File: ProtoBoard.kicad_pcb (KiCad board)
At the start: 4 copper layers, 68.2 x 45 mm, 56 parts, among them J1 Conn_01x02_Female, J10 Conn_01x06_Female, J2 Conn_01x10_Female, J3 I2C_STANDARDQWIIC, J4 Conn_01x10_Female, J5 Conn_01x05_Female, J6 Conn_01x05_Female, J7 Conn_01x10_Female, J8 Conn_01x05_Female, J9 Conn_01x10_Female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

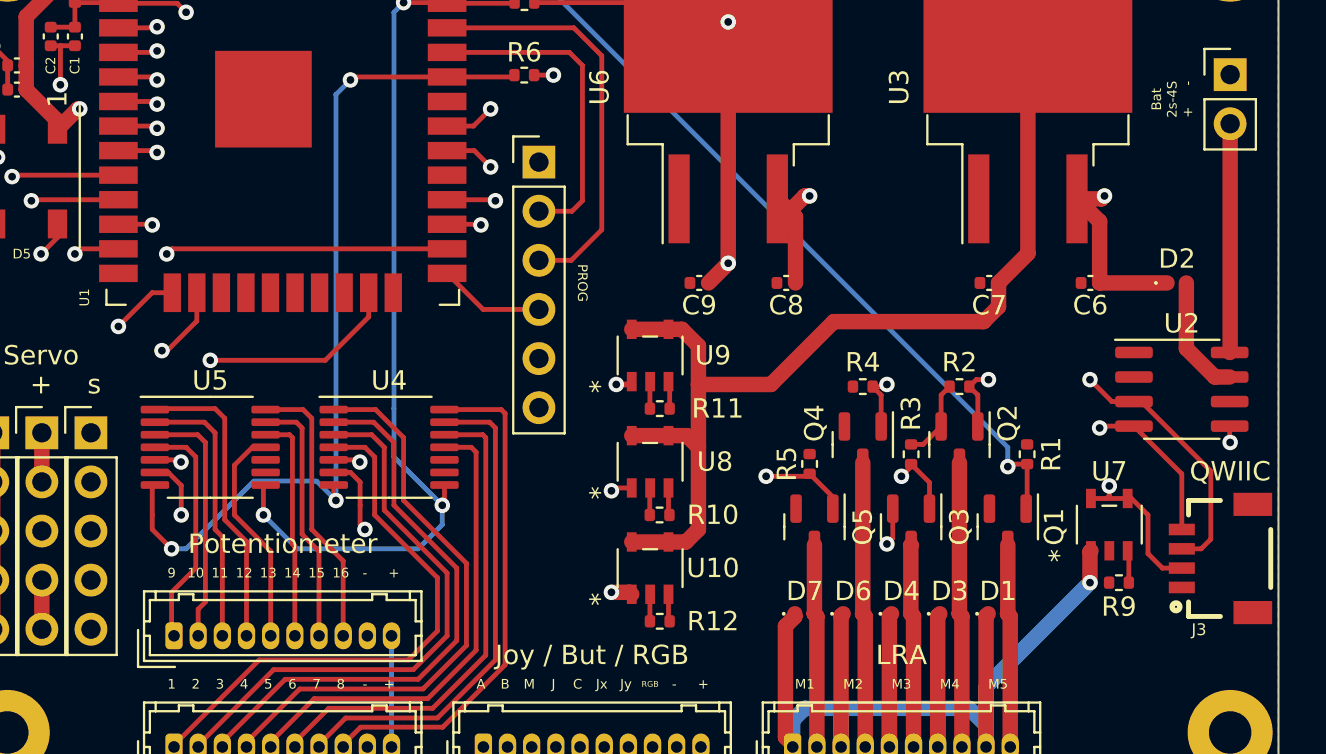
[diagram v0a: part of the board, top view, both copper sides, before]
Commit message: add shunt resistor and set i2c addresses
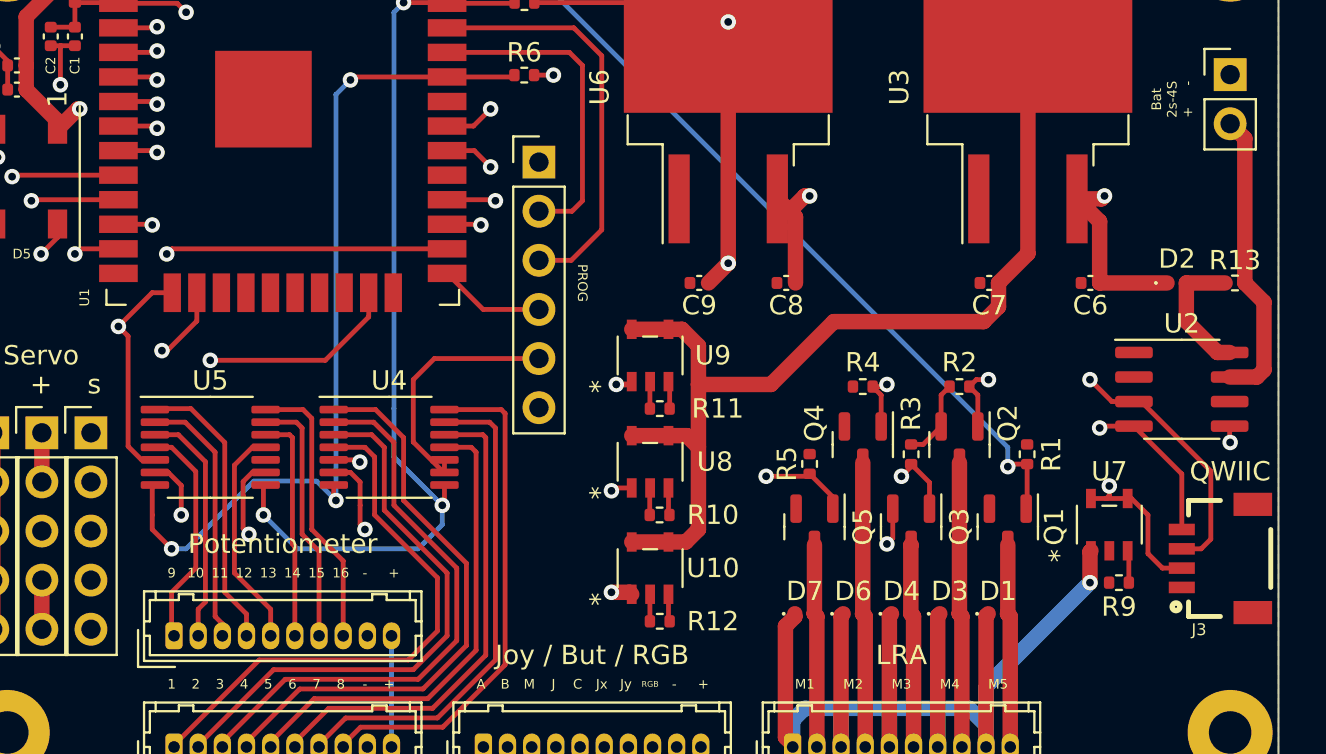
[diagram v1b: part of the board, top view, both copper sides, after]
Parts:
- added R13: 0.01R, Resistor_SMD:R_0402_1005Metric, F.Cu at (123.5, 69.2)
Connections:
- D2 pad 2: Net-(D2-Pad2) -> Net-(U2-Pad8)
- J1 pad 2: Net-(J1-Pad2) -> Net-(U2-Pad7)
- U2 pad 1: unconnected-(U2-Pad1) -> GND
- U2 pad 2: unconnected-(U2-Pad2) -> GND
- U2 pad 7: Net-(D2-Pad2) -> Net-(U2-Pad7)
- U2 pad 8: Net-(J1-Pad2) -> Net-(U2-Pad8)
- U4 pad 10: unconnected-(U4-Pad10) -> GND
- U4 pad 9: unconnected-(U4-Pad9) -> GND
- U5 pad 9: unconnected-(U5-Pad9) -> GND
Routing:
- net GND: track 34.4 -> 58.4 mm
- net Net-(U2-Pad7): track 0.00 -> 15.4 mm
- net Net-(J1-Pad2): track 11.8 -> 0.00 mm
- net Net-(U2-Pad8): track 0.00 -> 6.90 mm
- net Net-(D2-Pad2): track 6.24 -> 0.00 mm
- net /CH12: track 15.6 -> 14.8 mm
- net /CH11: track 14.0 -> 13.4 mm
- net /CH10: track 12.9 -> 12.3 mm

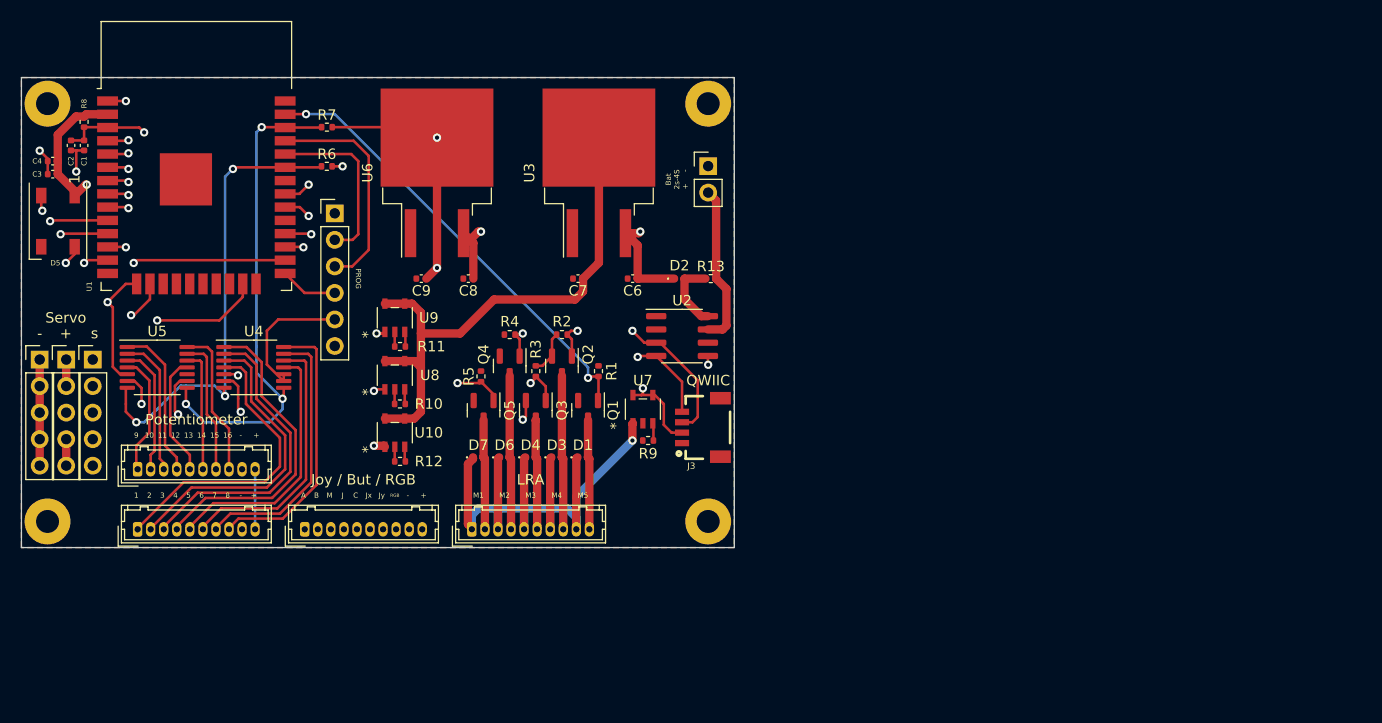
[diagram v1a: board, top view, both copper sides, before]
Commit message: smaller (but more expensive) version board
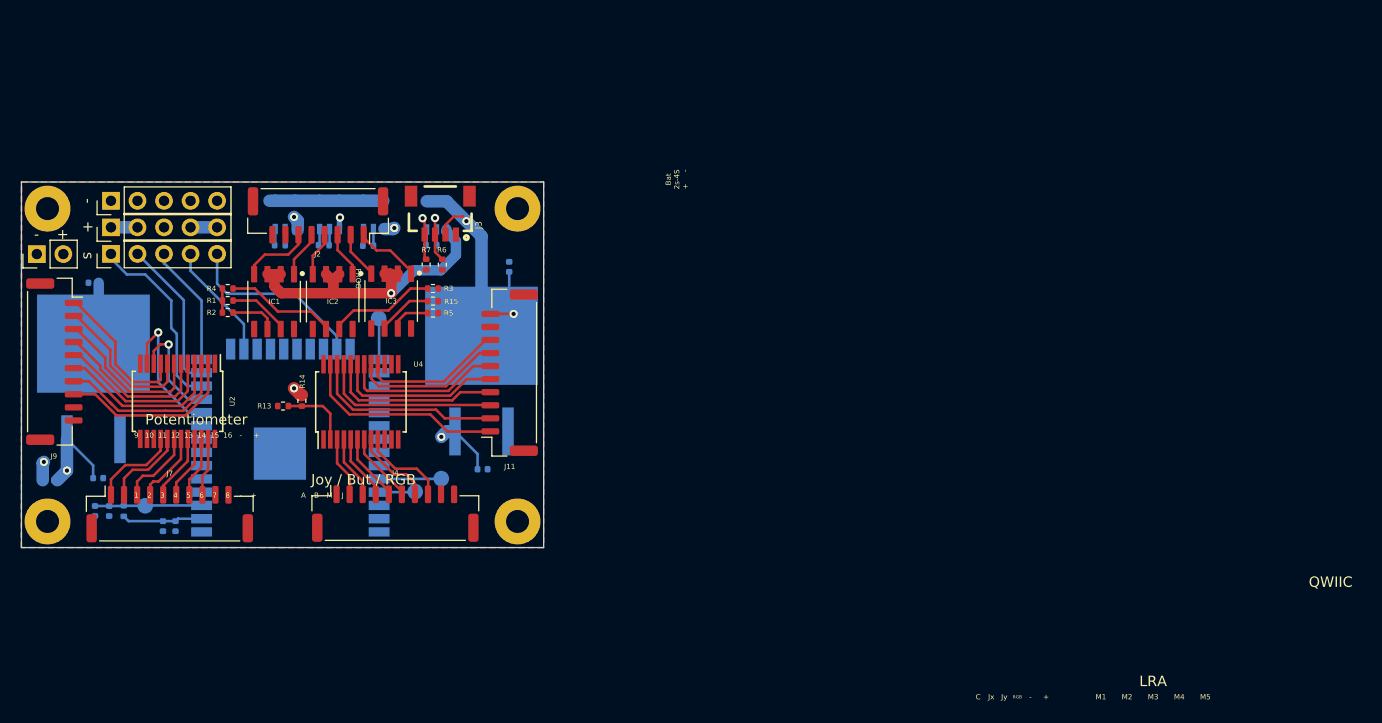
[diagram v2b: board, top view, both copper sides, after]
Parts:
- removed D1, D3, D4, D6, D7: D, Diode_SMD:D_0402_1005Metric
- removed D5: WS2812B, LED_SMD:LED_WS2812B_PLCC4_5.0x5.0mm_P3.2mm
- removed J10: Conn_01x06_Female, Connector_PinHeader_2.54mm:PinHeader_1x06_P2.54mm_Vertical
- removed Q1, Q2, Q3, Q4, Q5: 2N7002, Package_TO_SOT_SMD:SOT-23
- removed U5: MCP3428, Package_SO:TSSOP-14_4.4x5mm_P0.65mm
- added IC1: L9110S, footprints:SOIC127P600X150-8, F.Cu at (81.7, 71.5)
- added IC2: L9110S, footprints:SOIC127P600X150-8, F.Cu at (87.3, 71.5)
- added IC3: L9110S, footprints:SOIC127P600X150-8, F.Cu at (92.9, 71.4)
- added J11: Conn_01x10_Female, Connector_JST:JST_GH_SM10B-GHS-TB_1x10-1MP_P1.25mm_Horizontal, F.Cu at (104.2, 78.2)
- added R14: 1M, Resistor_SMD:R_0402_1005Metric, F.Cu at (84.3, 81.0)
- added R15: 10K, Resistor_SMD:R_0402_1005Metric, F.Cu at (96.9, 71.4)
- added TP1: TestPoint, TestPoint:TestPoint_Pad_D1.5mm, B.Cu at (69.3, 91.0)
- added TP2: TestPoint, TestPoint:TestPoint_Pad_D1.5mm, B.Cu at (97.7, 88.4)
- added TP3: TestPoint, TestPoint:TestPoint_Pad_D1.5mm, B.Cu at (95.2, 89.7)
- added TP4: TestPoint, TestPoint:TestPoint_Pad_D1.5mm, B.Cu at (91.7, 73.0)
- C1, C2, C3, C4, C6, C7, C8, C9, D2, R10, R11, R12, R8, R9, U1, U10, U3, U6, U7, U8, U9: moved to B.Cu
- J2: value Conn_01x10_Female -> Conn_01x08_Female; footprint Connector_Hirose:Hirose_DF13-10P-1.25DSA_1x10_P1.25mm_Vertical -> Connector_JST:JST_GH_SM08B-GHS-TB_1x08-1MP_P1.25mm_Horizontal
- J4, J7, J9: footprint Connector_Hirose:Hirose_DF13-10P-1.25DSA_1x10_P1.25mm_Vertical -> Connector_JST:JST_GH_SM10B-GHS-TB_1x10-1MP_P1.25mm_Horizontal
- R1, R2, R3, R4, R5: value 100K -> 10K
- R13: value 0.01R -> 6M
- U2: value INA219AxD -> CD74HC4067SM; footprint Package_SO:SOIC-8_3.9x4.9mm_P1.27mm -> Package_SO:SSOP-24_5.3x8.2mm_P0.65mm
- U4: value MCP3428 -> CD74HC4067SM; footprint Package_SO:TSSOP-14_4.4x5mm_P0.65mm -> Package_SO:SSOP-24_5.3x8.2mm_P0.65mm
- moved J1 64.8 mm to (59.0, 66.9), turned to 90 degrees
- moved D2 63.4 mm to (60.1, 88.5), turned to 180 degrees
- moved C6 54.6 mm to (64.8, 88.3), turned to 0 degrees
- moved U3 52.3 mm to (64.4, 78.8)
- moved U2 48.7 mm to (72.5, 81.0), turned to -90 degrees
- moved C7 46.4 mm to (64.4, 69.7)
- moved R13 42.7 mm to (82.5, 81.5), turned to 180 degrees
- moved R8 37.5 mm to (67.3, 91.5), turned to 90 degrees
- moved C4 36.5 mm to (71.0, 93.0), turned to -90 degrees
- moved R1 36.1 mm to (77.2, 71.3), turned to 180 degrees
- moved C3 35.7 mm to (72.2, 93.0), turned to -90 degrees
- moved C2 35.2 mm to (65.9, 91.5)
- moved C1 35.0 mm to (64.5, 91.5)
- moved J2 33.5 mm to (85.9, 63.2), turned to 180 degrees
- moved R2 32.1 mm to (77.2, 72.5)
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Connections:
- D2 pad 2: Net-(U2-Pad8) -> Net-(D2-Pad2)
- J1 pad 2: Net-(U2-Pad7) -> Net-(D2-Pad2)
- J2 pad 1: /POWER4 -> /M1+
- J2 pad 2: /M1- -> /M2+
- J2 pad 3: /POWER4 -> /M3+
- J2 pad 4: /M2- -> /M4+
- J2 pad 5: /POWER4 -> /M5+
- J2 pad 6: /M3- -> /M6+
- J2 pad 7: /POWER4 -> GND
- J2 pad 8: /M4- -> GND
- J4 pad 1: /ButA -> /RGB
- J4 pad 2: Net-(D5-Pad2) -> /ButA
- J7 pad 1: /CH1 -> /CH16
- J7 pad 2: /CH2 -> /CH15
- J7 pad 3: /CH3 -> /CH14
- J7 pad 4: /CH4 -> /CH13
- J7 pad 5: /CH5 -> /CH12
- J7 pad 6: /CH6 -> /CH11
- J7 pad 7: /CH7 -> /CH10
- J7 pad 8: /CH8 -> /CH9
- J8 pad 1: /S9 -> /S11
- J9 pad 1: /CH9 -> /CH1
- J9 pad 2: /CH10 -> /CH2
- J9 pad 3: /CH11 -> /CH3
- J9 pad 4: /CH12 -> /CH4
- J9 pad 5: /CH13 -> /CH5
- J9 pad 6: /CH14 -> /CH6
- J9 pad 7: /CH15 -> /CH7
- J9 pad 8: /CH16 -> /CH8
- R1 pad 2: GND -> +3V3
- R13 pad 1: Net-(U2-Pad8) -> Net-(R13-Pad1)
- R13 pad 2: Net-(U2-Pad7) -> GND
- R2 pad 1: /S7 -> /S9
- R2 pad 2: GND -> +3V3
- R3 pad 2: GND -> +3V3
- R4 pad 1: /S5 -> /S7
- R4 pad 2: GND -> +3V3
- R5 pad 2: GND -> +3V3
- U1 pad 10: /S9 -> /SEL2
- U1 pad 11: /S10 -> /SEL1
- U1 pad 12: /ButA -> /S11
- U1 pad 13: /S2 -> /S10
- U1 pad 14: unconnected-(U1-Pad14) -> /S2
- U1 pad 29: unconnected-(U1-Pad29) -> /S9
- U1 pad 4: /JoyX -> unconnected-(U1-Pad4)
- U1 pad 5: /JoyY -> unconnected-(U1-Pad5)
- U1 pad 6: /ButJ -> unconnected-(U1-Pad6)
- U1 pad 7: /ButC -> unconnected-(U1-Pad7)
- U1 pad 8: /ButB -> /SEL3
- U1 pad 9: /Menu -> /SEL4
- U2 pad 2: GND -> /CH8
- U2 pad 3: /I2C_SDA -> /CH7
- U2 pad 4: /I2C_SCL -> /CH6
- U2 pad 5: +3V3 -> /CH5
- U2 pad 6: GND -> /CH4
- U2 pad 7: Net-(U2-Pad7) -> /CH3
- U2 pad 8: Net-(U2-Pad8) -> /CH2
- U4 pad 1: /CH4 -> GND
- U4 pad 10: GND -> /SEL1
- U4 pad 11: /CH5 -> /SEL2
- U4 pad 12: /CH6 -> GND
- U4 pad 13: /CH7 -> /SEL4
- U4 pad 14: /CH8 -> /SEL3
- U4 pad 2: /CH3 -> Net-(R13-Pad1)
- U4 pad 3: /CH2 -> /ButA
- U4 pad 4: /CH1 -> /Menu
- U4 pad 5: GND -> /ButB
- U4 pad 6: +3V3 -> /ButC
- U4 pad 7: /I2C_SDA -> /ButJ
- U4 pad 8: /I2C_SCL -> /JoyY
- U4 pad 9: GND -> /JoyX
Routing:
- net +3V3: track 211.3 -> 39.2 mm, vias 8 -> 2
- net /I2C_SDA: track 105.4 -> 4.24 mm, vias 4 -> 1
- net /I2C_SCL: track 104.3 -> 4.06 mm, vias 4 -> 1
- net /POWER4: track 103.2 -> 33.2 mm
- net GND: track 58.4 -> 6.22 mm, vias 7 -> 0
- net Net-(D5-Pad2): track 47.0 -> 0.00 mm, vias 1 -> 0
- net /JoyX: track 49.9 -> 8.46 mm, vias 1 -> 0
- net /JoyY: track 48.1 -> 7.66 mm, vias 1 -> 0
- net /ButJ: track 46.1 -> 6.74 mm, vias 1 -> 0
- net +5V: track 60.4 -> 21.6 mm
- net /ButC: track 44.4 -> 6.49 mm, vias 1 -> 0
- net /S8: track 43.4 -> 5.92 mm, vias 2 -> 0
- net /ButB: track 42.6 -> 6.24 mm, vias 1 -> 0
- net /Menu: track 40.8 -> 6.00 mm, vias 1 -> 0
- net /ButA: track 36.7 -> 5.75 mm, vias 1 -> 0
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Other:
- board size 68.2 x 45 mm -> 50 x 35 mm
- board text removed: "Servo"

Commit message: Board cleaning progress
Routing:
- net +3V3: track 39.2 -> 144.3 mm, vias 2 -> 4
- net /SEL3: track 0.00 -> 69.0 mm, vias 0 -> 2
- net /RGB: track 0.00 -> 56.6 mm, vias 0 -> 2
- net /SEL4: track 0.00 -> 52.2 mm, vias 0 -> 4
- net GND: track 6.22 -> 47.9 mm, vias 0 -> 8
- net /I2C_SCL: track 4.06 -> 41.5 mm, vias 1 -> 2
- net /I2C_SDA: track 4.24 -> 38.6 mm, vias 1 -> 2
- net /SEL2: track 13.6 -> 46.0 mm, vias 1 -> 2
- net /S8: track 5.92 -> 37.4 mm, vias 0 -> 2
- net /S7: track 10.6 -> 41.1 mm, vias 0 -> 1
- net /SEL1: track 10.2 -> 36.1 mm, vias 1 -> 2
- net +5V: track 21.6 -> 46.1 mm
- net /S4: track 3.88 -> 25.9 mm, vias 0 -> 2
- net /S5: track 5.35 -> 22.8 mm, vias 0 -> 1
- net /S6: track 10.3 -> 26.3 mm, vias 0 -> 1
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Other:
- board text removed: "1"
- board text removed: "10"
- board text removed: "11"
- board text removed: "12"
- board text removed: "13"
- board text removed: "14"
- board text removed: "15"
- board text removed: "16"
- board text removed: "2"
- board text removed: "3"
- board text removed: "4"
- board text removed: "5"
- board text removed: "6"
- board text removed: "7"
- board text removed: "8"
- board text removed: "9"
- board text removed: "A"
- board text removed: "B"
- board text removed: "Bat 2s-4S + -"
- board text removed: "C"
- board text removed: "J"
- board text removed: "Joy / But / RGB"
- board text removed: "Jx"
- board text removed: "Jy"
- board text removed: "LRA"
- board text removed: "M"
- board text removed: "M1"
- board text removed: "M2"
- board text removed: "M3"
- board text removed: "M4"
- board text removed: "M5"
- board text removed: "PROG"
- board text removed: "Potentiometer"
- board text removed: "QWIIC"
- board text removed: "RGB"

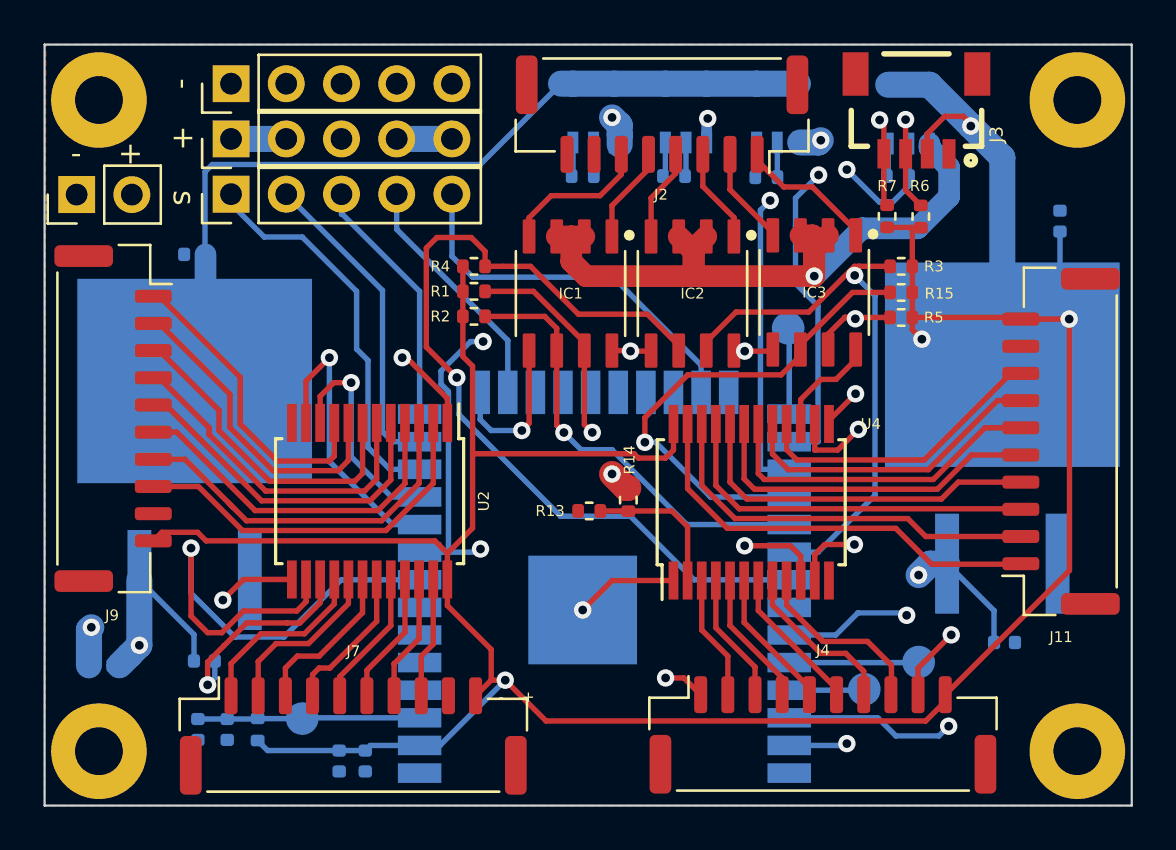
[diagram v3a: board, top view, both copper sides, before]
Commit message: More pcb cleaning
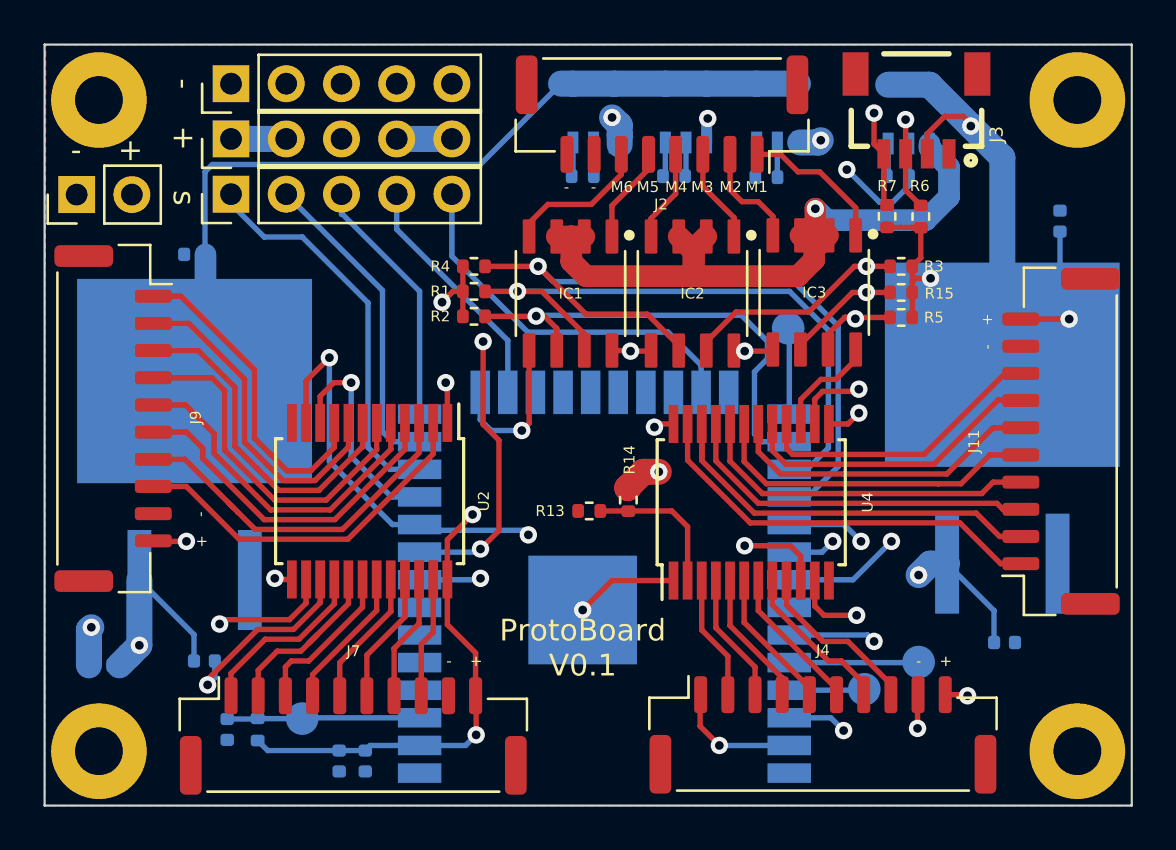
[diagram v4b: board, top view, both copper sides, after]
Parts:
- removed C1: C, Capacitor_SMD:C_0402_1005Metric
- C2, C4: value C -> 0.1uF
- C3: value C -> 22uF
- R11: value 3.4K -> 6.8K
- R13: value 6M -> 1M
- R14: value 1M -> 5M
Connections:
- net /S1 renamed /Servo4
- net /S10 renamed /Servo2
- net /S11 renamed /Servo1
- net /S2 renamed /Servo3
- net /S3 renamed /Servo5
- IC1 pad 6: /S9 -> /LRA6
- IC1 pad 7: /S8 -> /LRA5
- IC2 pad 6: /S7 -> /LRA4
- IC2 pad 7: /S6 -> /LRA3
- IC3 pad 6: /S5 -> /LRA2
- IC3 pad 7: /S4 -> /LRA1
- R1 pad 1: /S8 -> /LRA5
- R15 pad 1: /S5 -> /LRA2
- R2 pad 1: /S9 -> /LRA6
- R3 pad 1: /S6 -> /LRA3
- R4 pad 1: /S7 -> /LRA4
- R5 pad 1: /S4 -> /LRA1
- U1 pad 26: /RGB -> /LRA6
- U1 pad 27: /S4 -> /LRA5
- U1 pad 28: /S5 -> /LRA4
- U1 pad 29: /S9 -> /LRA2
- U1 pad 30: /S6 -> /LRA1
- U1 pad 31: /S7 -> /LRA3
- U1 pad 37: /S8 -> /RGB
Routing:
- net /RGB: track 56.6 -> 5.93 mm, vias 2 -> 1
- net /S7: track 41.1 -> 0.00 mm, vias 1 -> 0
- net /S8: track 37.4 -> 0.00 mm, vias 2 -> 0
- net /LRA4: track 0.00 -> 34.9 mm, vias 0 -> 1
- net /LRA3: track 0.00 -> 30.2 mm, vias 0 -> 2
- net /LRA5: track 0.00 -> 28.8 mm, vias 0 -> 1
- net /S6: track 26.3 -> 0.00 mm, vias 1 -> 0
- net /S4: track 25.9 -> 0.00 mm, vias 2 -> 0
- net /S5: track 22.8 -> 0.00 mm, vias 1 -> 0
- net /LRA6: track 0.00 -> 22.0 mm, vias 0 -> 1
- net /LRA2: track 0.00 -> 21.8 mm, vias 0 -> 2
- net /S9: track 20.6 -> 0.00 mm, vias 1 -> 0
- net /LRA1: track 0.00 -> 18.6 mm, vias 0 -> 2
- net +BATT: track 59.4 -> 67.9 mm
- net /SEL4: track 52.2 -> 44.1 mm
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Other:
- board text added: "M1"
- board text added: "M2"
- board text added: "M3"
- board text added: "M4"
- board text added: "M5"
- board text added: "M6"
- board text added: "ProtoBoard V0.1"
